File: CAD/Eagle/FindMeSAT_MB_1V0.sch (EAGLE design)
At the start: 128 parts, among them J291 MCX-J-P-X-RA-SM1, J685 SMA_CON, J701 MOLEX_105017-0001, J801 MICROSIM-8P_SDCARD-8P_MOLEX-1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, J901 JST_S3B-XH-A, Q101 ABS07-32.768KHZ, Q651 ABM3B-16MHZ-10-R50-1-U, U1001 CFPT-141-20MHZ, U101 ATXMEGA256A3BU-AU, U1011 OPA354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

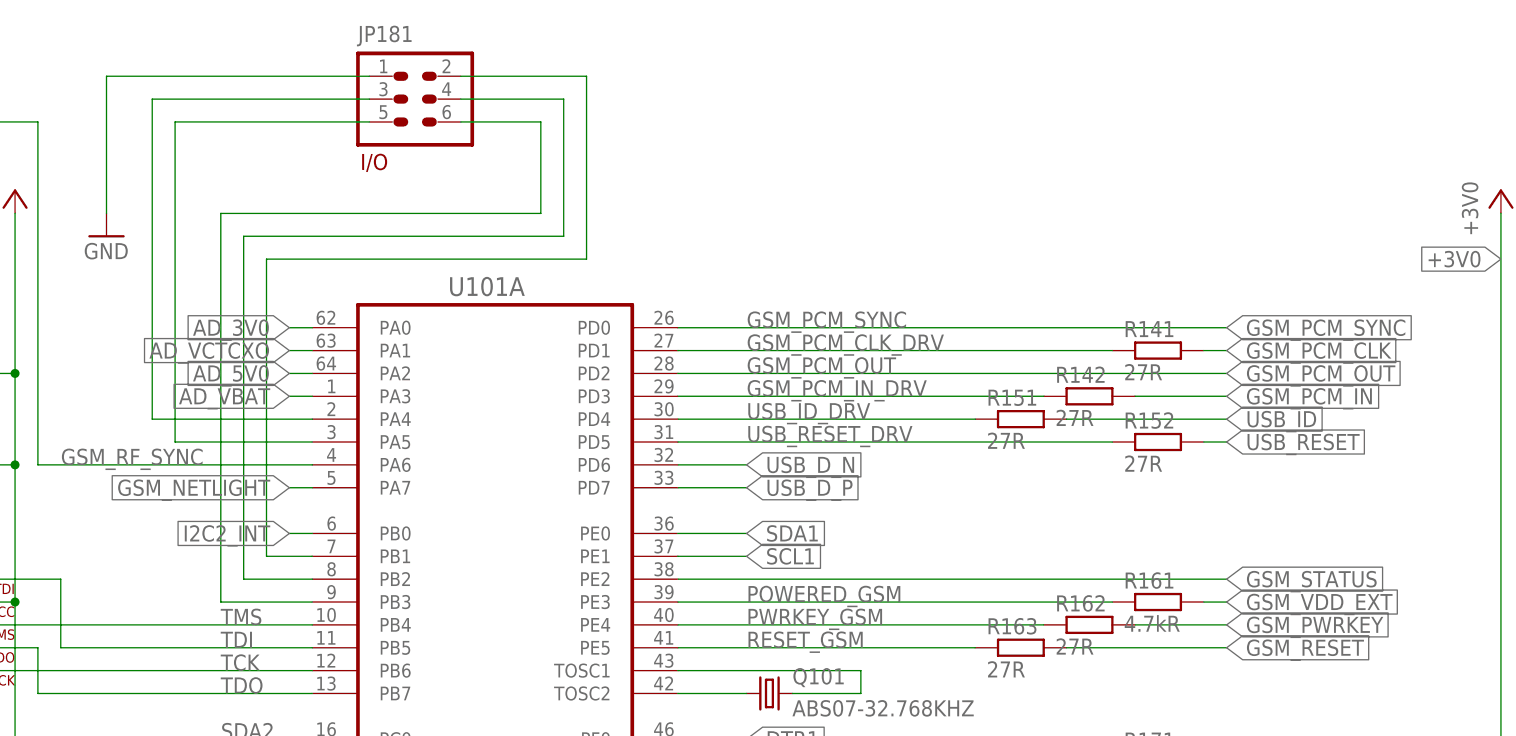
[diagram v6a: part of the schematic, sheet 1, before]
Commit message: Eagle - I/O header needs OC1A for digital clock output, USB_ID gives way and goes to ADC1/ADC9/AC1 port
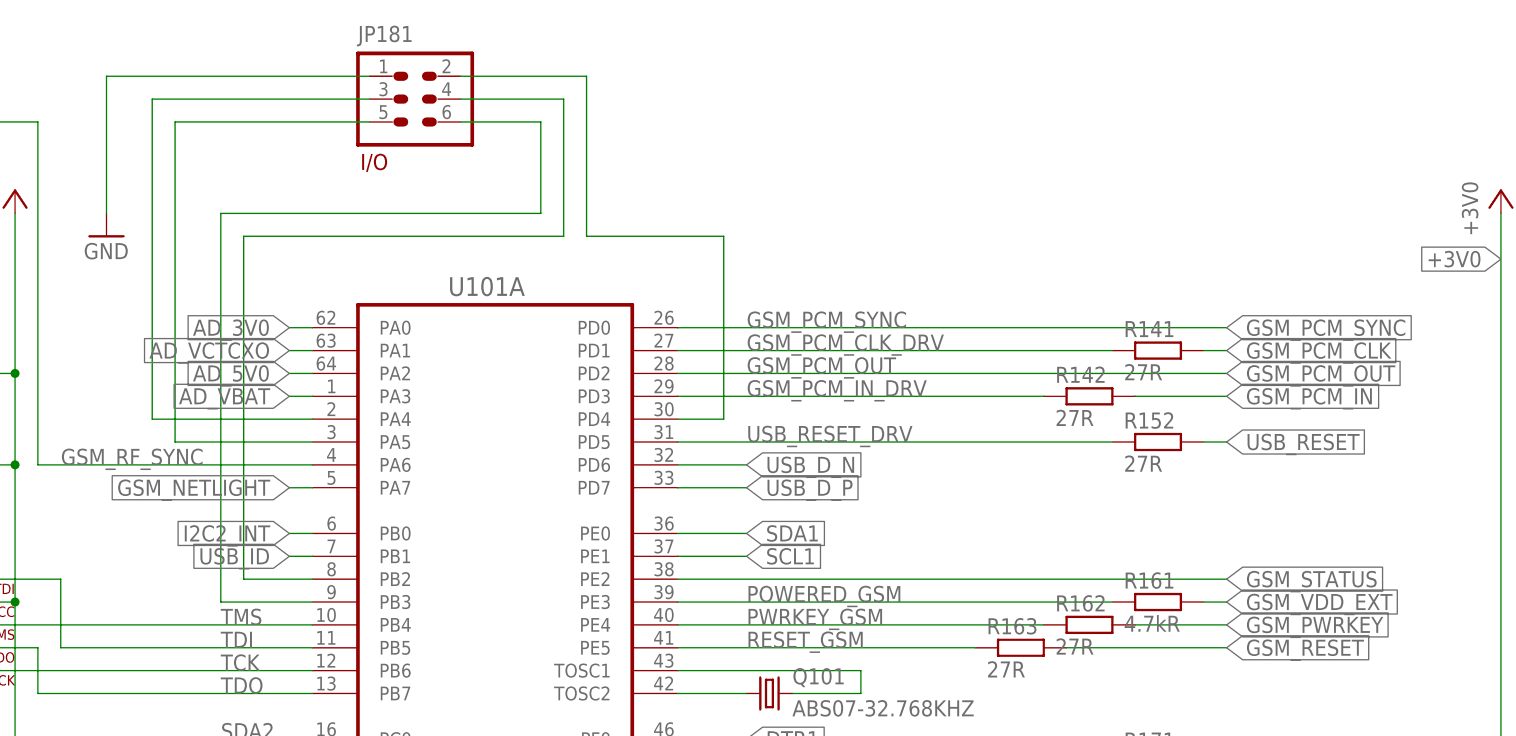
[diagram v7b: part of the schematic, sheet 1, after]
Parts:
- removed R151: 27R, rcl:R-EU_R0603
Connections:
- net IO_AD1 renamed IO_ADC4
- net IO_AD2 renamed IO_ADC5
- net IO_D2 renamed IO_DAC0
- net IO_D3 renamed IO_DAC1
- removed net IO_D1: JP181.2, U101A.PB1
- removed net USB_ID_DRV: R151.1, U101A.PD4
- new net IO_OC1A: JP181.2, U101A.PD4
- net USB_ID: now also U101A.PB1; no longer R151.2
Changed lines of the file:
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@@
 <part name="+3V3_121" library="df4iah_supply" deviceset="+3V3" device=""/>
 <part name="R251" library="rcl" deviceset="R-EU_" device="R0603" value="27R"/>
-<part name="R151" library="rcl" deviceset="R-EU_" device="R0603" value="27R"/>
 <part name="R152" library="rcl" deviceset="R-EU_" device="R0603" value="27R"/>
 <part name="C141" library="rcl" deviceset="C-EU" device="C0603" value="100pF"/>
@@
 <instance part="R142" gate="G$1" x="175.26" y="132.08"/>
 <instance part="+3V3_121" gate="G$1" x="55.88" y="154.94"/>
-<instance part="R151" gate="G$1" x="167.64" y="129.54"/>
 <instance part="R152" gate="G$1" x="182.88" y="127"/>
 <instance part="C141" gate="G$1" x="40.64" y="154.94"/>
@@
 </segment>
 </net>
-<net name="USB_ID" class="0">
-<segment>
-<wire x1="172.72" y1="129.54" x2="190.5" y2="129.54" width="0.1524" layer="91"/>
-<label x="190.5" y="129.54" size="1.778" layer="95" xref="yes"/>
-<pinref part="R151" gate="G$1" pin="2"/>
-</segment>
-</net>
-<net name="USB_ID_DRV" class="0">
-<segment>
-<pinref part="R151" gate="G$1" pin="1"/>
-<pinref part="U101" gate="A" pin="PD4"/>
-<wire x1="162.56" y1="129.54" x2="129.54" y2="129.54" width="0.1524" layer="91"/>
-<label x="137.16" y="129.54" size="1.778" layer="95"/>
-</segment>
-</net>
 <net name="GSM_RF_SYNC" class="0">
 <segment>
@@
 </segment>
 </net>
-<net name="IO_AD1" class="0">
+<net name="IO_ADC4" class="0">
 <segment>
 <pinref part="U101" gate="A" pin="PA4"/>
@@
 </segment>
 </net>
-<net name="IO_AD2" class="0">
+<net name="IO_ADC5" class="0">
 <segment>
 <pinref part="U101" gate="A" pin="PA5"/>
@@
 </segment>
 </net>
-<net name="IO_D1" class="0">
-<segment>
-<pinref part="U101" gate="A" pin="PB1"/>
-<wire x1="88.9" y1="114.3" x2="83.82" y2="114.3" width="0.1524" layer="91"/>
-<wire x1="83.82" y1="114.3" x2="83.82" y2="147.32" width="0.1524" layer="91"/>
-<wire x1="83.82" y1="147.32" x2="119.38" y2="147.32" width="0.1524" layer="91"/>
-<wire x1="119.38" y1="147.32" x2="119.38" y2="167.64" width="0.1524" layer="91"/>
+<net name="IO_OC1A" class="0">
+<segment>
+<wire x1="119.38" y1="149.86" x2="119.38" y2="167.64" width="0.1524" layer="91"/>
 <wire x1="119.38" y1="167.64" x2="105.41" y2="167.64" width="0.1524" layer="91"/>
 <pinref part="JP181" gate="G$1" pin="2"/>
-</segment>
-</net>
-<net name="IO_D2" class="0">
+<wire x1="119.38" y1="149.86" x2="134.62" y2="149.86" width="0.1524" layer="91"/>
+<wire x1="134.62" y1="149.86" x2="134.62" y2="129.54" width="0.1524" layer="91"/>
+<pinref part="U101" gate="A" pin="PD4"/>
+<wire x1="134.62" y1="129.54" x2="129.54" y2="129.54" width="0.1524" layer="91"/>
+</segment>
+</net>
+<net name="IO_DAC0" class="0">
 <segment>
 <pinref part="U101" gate="A" pin="PB2"/>
@@
 </segment>
 </net>
-<net name="IO_D3" class="0">
+<net name="IO_DAC1" class="0">
 <segment>
 <pinref part="U101" gate="A" pin="PB3"/>
@@
 </segment>
 </net>
+<net name="USB_ID" class="0">
+<segment>
+<pinref part="U101" gate="A" pin="PB1"/>
+<wire x1="88.9" y1="114.3" x2="86.36" y2="114.3" width="0.1524" layer="91"/>
+<label x="86.36" y="114.3" size="1.778" layer="95" rot="R180" xref="yes"/>
+</segment>
+</net>

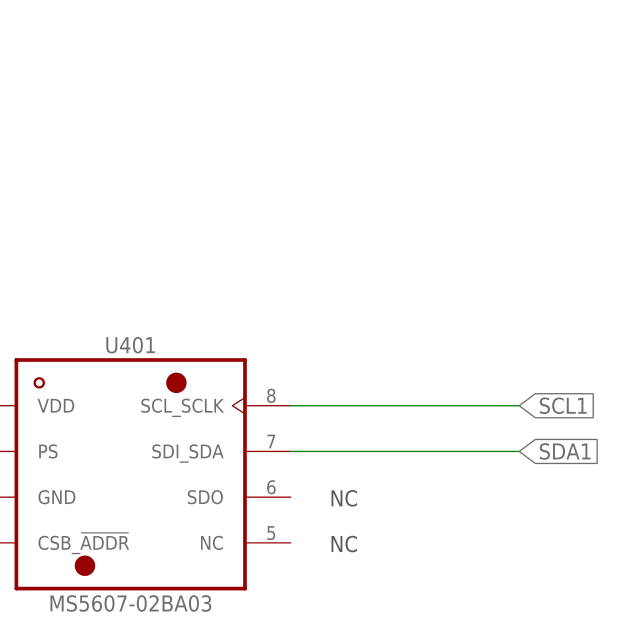
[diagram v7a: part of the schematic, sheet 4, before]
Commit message: Eagle - I2C bus terminated
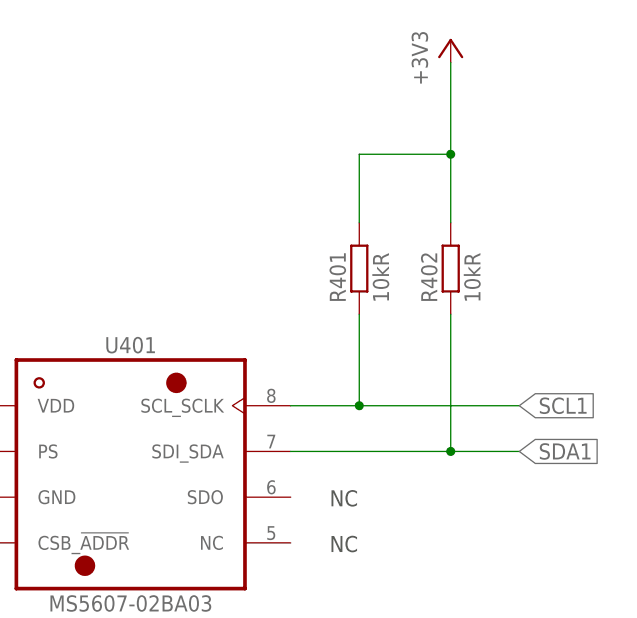
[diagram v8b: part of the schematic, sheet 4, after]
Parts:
- added R401, R402: 10kR, rcl:R-EU_R0603
- R211, R212: value 3.3kR -> 10kR
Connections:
- net +3V3: now also R401.2, R402.2
- net SCL1: now also R401.1
- net SDA1: now also R402.1
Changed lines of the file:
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@@
 <part name="R1131" library="rcl" deviceset="R-EU_" device="R0603" value="4.02kR"/>
 <part name="GND1131" library="df4iah_supply" deviceset="GND" device=""/>
-<part name="R211" library="rcl" deviceset="R-EU_" device="R0603" value="3.3kR"/>
-<part name="R212" library="rcl" deviceset="R-EU_" device="R0603" value="3.3kR"/>
+<part name="R211" library="rcl" deviceset="R-EU_" device="R0603" value="10kR"/>
+<part name="R212" library="rcl" deviceset="R-EU_" device="R0603" value="10kR"/>
 <part name="+3V3_211" library="df4iah_supply" deviceset="+3V3" device=""/>
 <part name="R172" library="rcl" deviceset="R-EU_" device="R0603" value="27R"/>
@@
 <part name="GND181" library="df4iah_supply" deviceset="GND" device=""/>
 <part name="U401" library="df4iah_sensors" deviceset="MS5607-02BA" device="" technology="03"/>
+<part name="R402" library="rcl" deviceset="R-EU_" device="R0603" value="10kR"/>
+<part name="R401" library="rcl" deviceset="R-EU_" device="R0603" value="10kR"/>
+<part name="+3V3_1" library="df4iah_supply" deviceset="+3V3" device=""/>
 </parts>
 <sheets>
@@
 <instance part="C401" gate="G$1" x="83.82" y="96.52" rot="MR0"/>
 <instance part="U401" gate="G$1" x="132.08" y="93.98"/>
+<instance part="R402" gate="G$1" x="167.64" y="116.84" rot="R90"/>
+<instance part="R401" gate="G$1" x="157.48" y="116.84" rot="R90"/>
+<instance part="+3V3_1" gate="G$1" x="167.64" y="142.24"/>
 </instances>
 <busses>
@@
 <junction x="109.22" y="96.52"/>
 </segment>
+<segment>
+<pinref part="+3V3_1" gate="G$1" pin="+3V3"/>
+<wire x1="167.64" y1="139.7" x2="167.64" y2="129.54" width="0.1524" layer="91"/>
+<wire x1="167.64" y1="129.54" x2="157.48" y2="129.54" width="0.1524" layer="91"/>
+<junction x="167.64" y="129.54"/>
+<pinref part="R401" gate="G$1" pin="2"/>
+<wire x1="157.48" y1="129.54" x2="157.48" y2="121.92" width="0.1524" layer="91"/>
+<pinref part="R402" gate="G$1" pin="2"/>
+<wire x1="167.64" y1="129.54" x2="167.64" y2="121.92" width="0.1524" layer="91"/>
+</segment>
 </net>
 <net name="SDA1" class="0">
 <segment>
-<wire x1="149.86" y1="96.52" x2="175.26" y2="96.52" width="0.1524" layer="91"/>
+<wire x1="149.86" y1="96.52" x2="167.64" y2="96.52" width="0.1524" layer="91"/>
 <label x="175.26" y="96.52" size="1.778" layer="95" xref="yes"/>
 <pinref part="U401" gate="G$1" pin="SDI_SDA"/>
+<wire x1="167.64" y1="96.52" x2="175.26" y2="96.52" width="0.1524" layer="91"/>
+<junction x="167.64" y="96.52"/>
+<pinref part="R402" gate="G$1" pin="1"/>
+<wire x1="167.64" y1="96.52" x2="167.64" y2="111.76" width="0.1524" layer="91"/>
 </segment>
 </net>
 <net name="SCL1" class="0">
 <segment>
-<wire x1="149.86" y1="101.6" x2="175.26" y2="101.6" width="0.1524" layer="91"/>
+<wire x1="149.86" y1="101.6" x2="157.48" y2="101.6" width="0.1524" layer="91"/>
 <label x="175.26" y="101.6" size="1.778" layer="95" xref="yes"/>
 <pinref part="U401" gate="G$1" pin="SCL_SCLK"/>
-</segment>
-</net>
+<wire x1="157.48" y1="101.6" x2="175.26" y2="101.6" width="0.1524" layer="91"/>
+<junction x="157.48" y="101.6"/>
+<pinref part="R401" gate="G$1" pin="1"/>
+<wire x1="157.48" y1="101.6" x2="157.48" y2="111.76" width="0.1524" layer="91"/>
+</segment>
+</net>
